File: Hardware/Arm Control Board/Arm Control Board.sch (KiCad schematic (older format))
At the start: 30 parts, among them P1 Servo 1, P10 UIM240XX_Stepper_Conn, P11 Battery, P12 SyRen, P13 Raspberry Pi, P2 Shoulder Feedback, P3 Servo 2, P4 Servo 3, P5 Elbow Feedback, P6 Servo 4, P7 RS485, P8 ST_SWD_Connector, P9 Servo 5, U1 STM32F401RCT6, U2 SN75176BDR, U3 74LVCH244APW, X1 24MHz

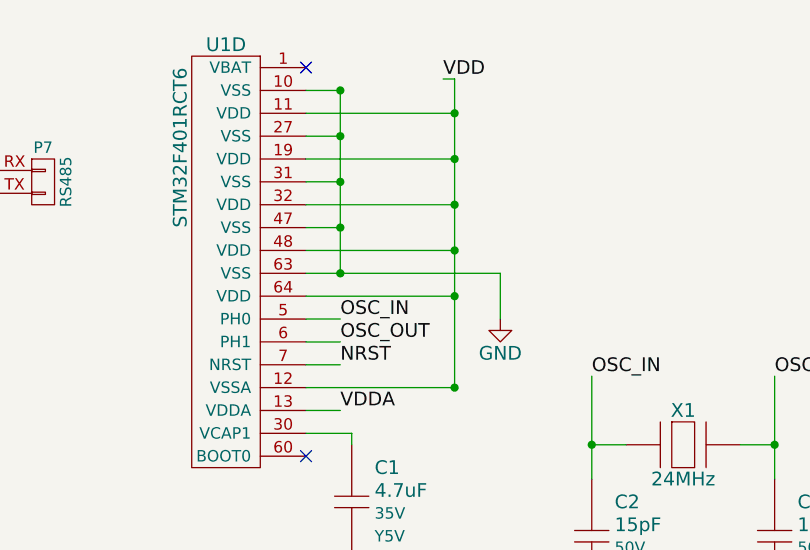
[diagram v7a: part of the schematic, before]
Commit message: all components have footprints assigned now
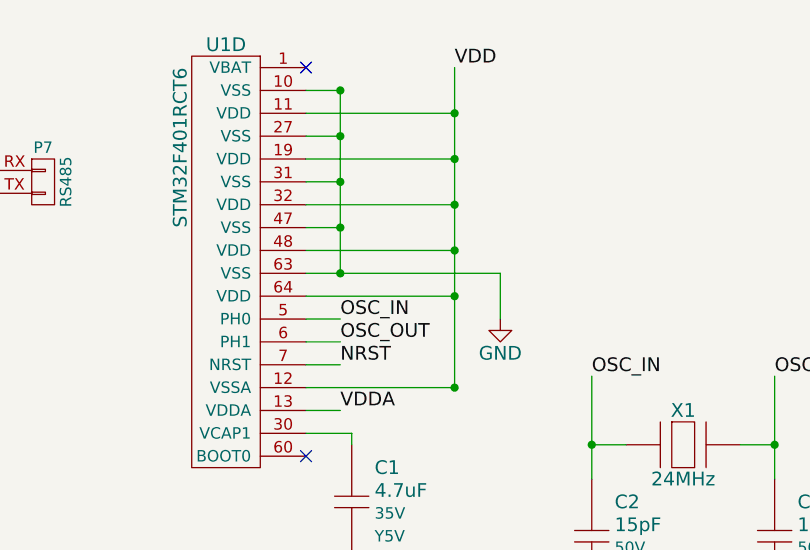
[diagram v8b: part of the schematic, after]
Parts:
- P1, P2, P3, P4, P5, P6, P9: footprint (none) -> MAVRIC_footprints:1x3_SMD_header
- P10, P8: footprint (none) -> MAVRIC_footprints:1x6_SMD_header
- P11: footprint (none) -> Wire_Pads:SolderWirePad_2x_2-5mmDrill
- P12, P13, P7: footprint (none) -> MAVRIC_footprints:1x2_SMD_header
- U1: footprint (none) -> Housings_QFP:LQFP-64_10x10mm_Pitch0.5mm
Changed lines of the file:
@@
 F 0 "P7" H 4650 1400 50  0000 C CNN
 F 1 "RS485" V 4750 1250 50  0000 C CNN
-F 2 "" H 4650 1250 60  0000 C CNN
+F 2 "MAVRIC_footprints:1x2_SMD_header" H 4650 1250 60  0001 C CNN
 F 3 "" H 4650 1250 60  0000 C CNN
 	1    4650 1250
@@
 F 0 "P11" H 8300 5950 50  0000 C CNN
 F 1 "Battery" V 8400 5800 50  0000 C CNN
-F 2 "" H 8300 5800 60  0000 C CNN
+F 2 "Wire_Pads:SolderWirePad_2x_2-5mmDrill" H 8300 5800 60  0001 C CNN
 F 3 "" H 8300 5800 60  0000 C CNN
 	1    8300 5800
@@
 F 0 "P1" H 800 7350 50  0000 C CNN
 F 1 "Servo 1" V 900 7150 50  0000 C CNN
-F 2 "" H 800 7150 60  0000 C CNN
+F 2 "MAVRIC_footprints:1x3_SMD_header" H 800 7150 60  0001 C CNN
 F 3 "" H 800 7150 60  0000 C CNN
 	1    800  7150
@@
 F 0 "P3" H 1900 7350 50  0000 C CNN
 F 1 "Servo 2" V 2000 7150 50  0000 C CNN
-F 2 "" H 1900 7150 60  0000 C CNN
+F 2 "MAVRIC_footprints:1x3_SMD_header" H 1900 7150 60  0001 C CNN
 F 3 "" H 1900 7150 60  0000 C CNN
 	1    1900 7150
@@
 F 0 "P4" H 3000 7350 50  0000 C CNN
 F 1 "Servo 3" V 3100 7150 50  0000 C CNN
-F 2 "" H 3000 7150 60  0000 C CNN
+F 2 "MAVRIC_footprints:1x3_SMD_header" H 3000 7150 60  0001 C CNN
 F 3 "" H 3000 7150 60  0000 C CNN
 	1    3000 7150
@@
 F 0 "P6" H 4050 7350 50  0000 C CNN
 F 1 "Servo 4" V 4150 7150 50  0000 C CNN
-F 2 "" H 4050 7150 60  0000 C CNN
+F 2 "MAVRIC_footprints:1x3_SMD_header" H 4050 7150 60  0001 C CNN
 F 3 "" H 4050 7150 60  0000 C CNN
 	1    4050 7150
@@
 F 0 "P9" H 5700 7350 50  0000 C CNN
 F 1 "Servo 5" V 5800 7150 50  0000 C CNN
-F 2 "" H 5700 7150 60  0000 C CNN
+F 2 "MAVRIC_footprints:1x3_SMD_header" H 5700 7150 60  0001 C CNN
 F 3 "" H 5700 7150 60  0000 C CNN
 	1    5700 7150
@@
 F 0 "U1" H 850 2900 60  0000 C CNN
 F 1 "STM32F401RCT6" V 650 2450 60  0000 C CNN
-F 2 "" H 1000 1200 60  0000 C CNN
+F 2 "Housings_QFP:LQFP-64_10x10mm_Pitch0.5mm" H 1000 1200 60  0001 C CNN
 F 3 "" H 1000 1200 60  0000 C CNN
 	2    1000 2800
@@
 F 0 "U1" H 850 4550 60  0000 C CNN
 F 1 "STM32F401RCT6" V 650 4100 60  0000 C CNN
-F 2 "" H 1000 2850 60  0000 C CNN
+F 2 "Housings_QFP:LQFP-64_10x10mm_Pitch0.5mm" H 1000 2850 60  0001 C CNN
 F 3 "" H 1000 2850 60  0000 C CNN
 	3    1000 4450
@@
 F 0 "P12" H 9450 5950 50  0000 C CNN
 F 1 "SyRen" V 9550 5800 50  0000 C CNN
-F 2 "" H 9450 5800 60  0000 C CNN
+F 2 "MAVRIC_footprints:1x2_SMD_header" H 9450 5800 60  0001 C CNN
 F 3 "" H 9450 5800 60  0000 C CNN
 	1    9450 5800
@@
 F 0 "P13" H 10450 5950 50  0000 C CNN
 F 1 "Raspberry Pi" V 10550 5800 50  0000 C CNN
-F 2 "" H 10450 5800 60  0000 C CNN
+F 2 "MAVRIC_footprints:1x2_SMD_header" H 10450 5800 60  0001 C CNN
 F 3 "" H 10450 5800 60  0000 C CNN
 	1    10450 5800
@@
 	1    0    0    -1
 $EndComp
-Text Label 6400 800  0    60   ~ 0
+Text Label 6450 750  0    60   ~ 0
 VDD
 $Comp
@@
 	5800 950  6450 950
 Wire Wire Line
-	5800 1750 6450 1750
+	6450 1750 5800 1750
 Connection ~ 6450 1750
 Wire Wire Line
-	5800 1550 6450 1550
+	6450 1550 5800 1550
 Connection ~ 6450 1550
 Wire Wire Line
-	5800 1350 6450 1350
+	6450 1350 5800 1350
 Connection ~ 6450 1350
 Wire Wire Line
-	5800 1150 6450 1150
+	6450 1150 5800 1150
 Connection ~ 6450 1150
 Wire Wire Line
@@
 F 0 "P10" H 7450 6200 50  0000 C CNN
 F 1 "UIM240XX_Stepper_Conn" V 7550 5850 50  0000 C CNN
-F 2 "" H 7450 5850 60  0000 C CNN
+F 2 "MAVRIC_footprints:1x6_SMD_header" H 7450 5850 60  0001 C CNN
 F 3 "" H 7450 5850 60  0000 C CNN
 	1    7450 5850
@@
 F 0 "P2" H 1900 6350 50  0000 C CNN
 F 1 "Shoulder Feedback" V 2000 6150 50  0000 C CNN
-F 2 "" H 1900 6150 60  0000 C CNN
+F 2 "MAVRIC_footprints:1x3_SMD_header" H 1900 6150 60  0001 C CNN
 F 3 "" H 1900 6150 60  0000 C CNN
 	1    1900 6150
@@
 F 0 "P5" H 3350 6350 50  0000 C CNN
 F 1 "Elbow Feedback" V 3450 6150 50  0000 C CNN
-F 2 "" H 3350 6150 60  0000 C CNN
+F 2 "MAVRIC_footprints:1x3_SMD_header" H 3350 6150 60  0001 C CNN
 F 3 "" H 3350 6150 60  0000 C CNN
 	1    3350 6150
@@
 F 0 "P8" H 5550 6200 50  0000 C CNN
 F 1 "ST_SWD_Connector" V 5650 5850 50  0000 C CNN
-F 2 "" H 5550 5850 60  0000 C CNN
+F 2 "MAVRIC_footprints:1x6_SMD_header" H 5550 5850 60  0001 C CNN
 F 3 "" H 5550 5850 60  0000 C CNN
 	1    5550 5850
@@
 $EndComp
 Wire Wire Line
-	6450 800  6450 2150
-Wire Wire Line
-	6450 800  6400 800
+	6450 750  6450 2150
 Connection ~ 6450 950
 Connection ~ 5950 1650
